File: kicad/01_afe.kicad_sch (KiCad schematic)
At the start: 0 parts

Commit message: Phase 1: sheet 1 (afe); power symbols for PGND/ISOPGND/DAB_GROUND groups on sheet 2
Co-Authored-By: Claude Fable 5.1 <noreply@anthropic.com>
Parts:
- added ACIN1, ACIN2, AFE_OUT, FILTER_IN, FILTER_OUT, J5, PE1, PE2, PE3, PE4: PIN, symbol ac_psu:PIN
- added C13, C14, C19, C20, C22, C23: 2n2, symbol ac_psu:C
- added C21, C24, C25: 7u, symbol ac_psu:C
- added C26: 100n, symbol ac_psu:C
- added CM1, CM2: WE-CMBNC, symbol ac_psu:WE-CMBNC
- added Q1, Q2, Q3, Q4: C3M0065090D, symbol ac_psu:C3M0065090D
- added R10: TWW10J15RE, symbol ac_psu:R
- added R11, R12, R13, R14, R15, R16, R2, R3, R4, R5, R6, R95: 91K, symbol ac_psu:R
- added R17, R21, R8: 10k, symbol ac_psu:R
- added R18, R9: 100, symbol ac_psu:R
- added R20: SLA-12VDC-SL-A, symbol ac_psu:SLA-12VDC-SL-A
- added R48: FKK5R0020FE-TR, symbol ac_psu:FKK5R0020FE-TR
- added R7: 1k, symbol ac_psu:R
- added U1: OPA2353UA, symbol ac_psu:OPA2353UA
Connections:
- new net: R3.1, R8.2, U1.6 (-)
- new net: R2.1, R3.2
- new net: R17.1, R18.2, U1.1
- new net: R16.1, R17.2, U1.2 (-)
- new net: R8.1, R9.2, U1.7
- new net: R12.2, R95.1
- new net: R4.1, R5.2
- new net: R15.1, R16.2
- new net: R14.1, R15.2
- new net: R12.1, R13.2
- new net: R11.1, R2.2
- new net: R6.1, R7.2, U1.5 (+)
- new net: R13.1, R21.2, U1.3 (+)
- new net: R5.1, R6.2
- new net 20V: R20.6 (COIL_2)
- new net AC_IN2: ACIN2.1, C14.2, C25.2, CM2.4, R95.2
- new net AC_IN_1: ACIN1.1, R10.1, R14.2, R20.3 (NO)
- new net ADA2: R18.1
- new net ADA3: R9.1
- new net CMFILT1: C22.2, C24.1, CM1.3, CM2.2
- new net CMFILT2: C23.2, C24.2, CM1.4, CM2.1
- new net DC+: Q1.2 (D), Q3.2 (D)
- new net FILTER_INPUT: C20.2, C21.2, CM1.1, FILTER_IN.1, R11.2
- new net G1_GATE_HI: Q1.1 (G)
- new net G1_SOURCE_HI: Q1.3 (S), Q2.2 (D), R48.4
- new net G2_GATE_LO: Q2.1 (G)
- new net G3_GATE_HI: Q3.1 (G)
- new net G3_SOURCE_HI: AFE_OUT.1, Q3.3 (S), Q4.2 (D)
- new net G4_GATE_LO: Q4.1 (G)
- new net GND: C26.1, U1.4 (V-)
- new net JEE: C13.2, C25.1, CM2.3, R10.2, R20.1 (COM_1)
- new net LEMOUT: C19.2, C21.1, CM1.2, FILTER_OUT.1, R4.2
- new net PE1: C19.1, C20.1, C23.1, PE1.1
- new net PE2: C14.1, PE2.1
- new net PE3: C22.1, PE3.1
- new net PE4: C13.1, PE4.1
- new net PGND: Q2.3 (S), Q4.3 (S)
- new net REF_1V65: R21.1, R7.1
- new net RELAY_DRIVE: R20.2 (COIL_1)
- new net SHUNT1: J5.1, R48.1, R48.3
- new net SHUNT2: R48.2
- new net VCC: C26.2, U1.8 (V+)
- no-connect marks 0 -> 1
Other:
- note added: "2 = SHUNT2 sense. U5 (sheet 8) floats on SHUNT1/SHUNT2."
- note added: "3V3 / DC- in the Proteus schematic = VCC / GND"
- note added: "AFE half bridges. Q2/Q4 sources are PGND (Proteus calls them G2_Source_LO / G4_Source_LO at J1)."
- note added: "EMI filter between the mains (ACIN1/ACIN2) and FILTER_IN/FILTER_OUT; R10 limits inrush until R20 closes."
- note added: "R48 2 mOhm shunt: 4 = Q1/Q2 midpoint, 1/3 = SHUNT1 -> J5 (afe_1_out_measured),"
- note added: "U1:A measures the mains voltage (AC_IN2 - AC_IN_1) around REF_1V65 -> ADA2."
- note added: "U1:B measures the filter voltage (LEMOUT - FILTER_INPUT) around REF_1V65 -> ADA3."

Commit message: Phase 2 done: footprints assigned and verified against IPC pads
- tools/gen_footprints.py -> lib/footprint_map.csv + lib/ac_psu.pretty (20 project footprints)
- tools/fpgeom.py: footprint pad loader and rigid fit; tools/check_footprints.py (+ pcbnew
  placement check), added to check_all.sh; reports/footprint_fit.csv for Phase 3 placement
- sch_builder: Footprint field from the map, deterministic UUIDs; all sheets regenerated
- kicad/fp-lib-table; STATUS.md (decisions, residuals, REF3025/C67 findings); Phase 3 prompt

Co-Authored-By: Claude Opus 5.5 <noreply@anthropic.com>
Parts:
- ACIN1, ACIN2: footprint (none) -> ac_psu:Terminal_2x1_P5.00mm_D2.0mm_Drill1.4mm
- AFE_OUT, FILTER_IN, FILTER_OUT, J5, PE3: footprint (none) -> ac_psu:Terminal_D4.0mm_Drill2.55mm
- C13, C14, C19, C20, C22, C23: footprint (none) -> Capacitor_THT:C_Disc_D12.5mm_W5.0mm_P7.50mm
- C21, C24, C25: footprint (none) -> Capacitor_THT:C_Rect_L33.0mm_W20.0mm_P27.50mm_MKS4
- C26: footprint (none) -> Capacitor_SMD:C_0402_1005Metric
- CM1, CM2: footprint (none) -> ac_psu:L_CommonMode_WE-CMBNC
- PE1: footprint (none) -> ac_psu:Terminal_D4.0mm_Drill3.0mm
- PE2, PE4: footprint (none) -> ac_psu:Terminal_D4.0mm_Drill2.0mm
- Q1, Q2, Q3, Q4: footprint (none) -> Package_TO_SOT_THT:TO-247-3_Vertical
- R10: footprint (none) -> Resistor_THT:R_Radial_Power_L13.0mm_W9.0mm_P5.00mm
- R11, R12, R13, R14, R15, R16, R2, R3, R4, R5, R6, R95: footprint (none) -> Resistor_SMD:R_1206_3216Metric_Pad1.30x1.75mm_HandSolder
- R17, R18, R21, R7, R8, R9: footprint (none) -> Resistor_SMD:R_0402_1005Metric
- R20: footprint (none) -> ac_psu:Relay_SLA-12VDC-SL-A
- R48: footprint (none) -> ac_psu:R_Shunt_FKK5R0020FE
- U1: footprint (none) -> Package_SO:TSSOP-8_3x3mm_P0.65mm
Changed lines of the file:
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@@
 			)
 		)
-		(property "Footprint" ""
+		(property "Footprint" "Package_TO_SOT_THT:TO-247-3_Vertical"
 			(at 55.88 48.26 0)
 			(effects
@@
 			)
 		)
-		(property "Footprint" ""
+		(property "Footprint" "Package_TO_SOT_THT:TO-247-3_Vertical"
 			(at 55.88 86.36 0)
 			(effects
@@
 			)
 		)
-		(property "Footprint" ""
+		(property "Footprint" "Package_TO_SOT_THT:TO-247-3_Vertical"
 			(at 106.68 48.26 0)
 			(effects
@@
 			)
 		)
-		(property "Footprint" ""
+		(property "Footprint" "Package_TO_SOT_THT:TO-247-3_Vertical"
 			(at 106.68 86.36 0)
 			(effects
@@
 			)
 		)
-		(property "Footprint" ""
+		(property "Footprint" "ac_psu:Terminal_D4.0mm_Drill2.55mm"
 			(at 119.38 74.93 0)
 			(effects
@@
 			)
 		)
-		(property "Footprint" ""
+		(property "Footprint" "ac_psu:R_Shunt_FKK5R0020FE"
 			(at 148.082 45.72 0)
 			(effects
@@
 			)
 		)
-		(property "Footprint" ""
+		(property "Footprint" "ac_psu:Terminal_D4.0mm_Drill2.55mm"
 			(at 160.02 48.26 0)
 			(effects
@@
 			)
 		)
-		(property "Footprint" ""
+		(property "Footprint" "ac_psu:Terminal_D4.0mm_Drill2.55mm"
 			(at 220.98 50.8 0)
 			(effects
@@
 			)
 		)
-		(property "Footprint" ""
+		(property "Footprint" "ac_psu:Terminal_D4.0mm_Drill2.55mm"
 			(at 210.82 60.96 0)
 			(effects
@@
 			)
 		)
-		(property "Footprint" ""
+		(property "Footprint" "Capacitor_THT:C_Disc_D12.5mm_W5.0mm_P7.50mm"
 			(at 224.4852 46.99 0)
 			(effects
@@
 			)
 		)
-		(property "Footprint" ""
+		(property "Footprint" "Capacitor_THT:C_Disc_D12.5mm_W5.0mm_P7.50mm"
 			(at 222.5548 64.77 0)
 			(effects
@@
 			)
 		)
-		(property "Footprint" ""
+		(property "Footprint" "Capacitor_THT:C_Rect_L33.0mm_W20.0mm_P27.50mm_MKS4"
 			(at 232.1052 59.69 0)
 			(effects
@@
 			)
 		)
-		(property "Footprint" ""
+		(property "Footprint" "ac_psu:L_CommonMode_WE-CMBNC"
 			(at 241.3 62.23 0)
 			(effects
@@
 			)
 		)
-		(property "Footprint" ""
+		(property "Footprint" "Capacitor_THT:C_Disc_D12.5mm_W5.0mm_P7.50mm"
 			(at 254.9652 46.99 0)
 			(effects
@@
 			)
 		)
-		(property "Footprint" ""
+		(property "Footprint" "Capacitor_THT:C_Disc_D12.5mm_W5.0mm_P7.50mm"
 			(at 253.0348 64.77 0)
 			(effects
@@
 			)
 		)
-		(property "Footprint" ""
+		(property "Footprint" "Capacitor_THT:C_Rect_L33.0mm_W20.0mm_P27.50mm_MKS4"
 			(at 262.5852 59.69 0)
 			(effects
@@
 			)
 		)
-		(property "Footprint" ""
+		(property "Footprint" "ac_psu:L_CommonMode_WE-CMBNC"
 			(at 271.78 62.23 0)
 			(effects
@@
 			)
 		)
-		(property "Footprint" ""
+		(property "Footprint" "Capacitor_THT:C_Rect_L33.0mm_W20.0mm_P27.50mm_MKS4"
 			(at 287.9852 59.69 0)
 			(effects
@@
 			)
 		)
-		(property "Footprint" ""
+		(property "Footprint" "Capacitor_THT:C_Disc_D12.5mm_W5.0mm_P7.50mm"
 			(at 295.6052 46.99 0)
 			(effects
@@
 			)
 		)
-		(property "Footprint" ""
+		(property "Footprint" "Capacitor_THT:C_Disc_D12.5mm_W5.0mm_P7.50mm"
 			(at 293.6748 64.77 0)
 			(effects
@@
 			)
 		)
-		(property "Footprint" ""
+		(property "Footprint" "Resistor_THT:R_Radial_Power_L13.0mm_W9.0mm_P5.00mm"
 			(at 300.482 35.56 0)
 			(effects
@@
 			)
 		)
-		(property "Footprint" ""
+		(property "Footprint" "ac_psu:Relay_SLA-12VDC-SL-A"
 			(at 274.32 22.86 0)
 			(effects
@@
 			)
 		)
-		(property "Footprint" ""
+		(property "Footprint" "ac_psu:Terminal_2x1_P5.00mm_D2.0mm_Drill1.4mm"
 			(at 312.42 25.4 0)
 			(effects
@@
 			)
 		)
-		(property "Footprint" ""
+		(property "Footprint" "ac_psu:Terminal_2x1_P5.00mm_D2.0mm_Drill1.4mm"
 			(at 312.42 66.04 0)
 			(effects
@@
 			)
 		)
-		(property "Footprint" ""
+		(property "Footprint" "Resistor_SMD:R_1206_3216Metric_Pad1.30x1.75mm_HandSolder"
 			(at 210.058 76.2 0)
 			(effects
@@
 			)
 		)
-		(property "Footprint" ""
+		(property "Footprint" "Resistor_SMD:R_1206_3216Metric_Pad1.30x1.75mm_HandSolder"
 			(at 210.058 86.36 0)
 			(effects
@@
 			)
 		)
-		(property "Footprint" ""
+		(property "Footprint" "Resistor_SMD:R_1206_3216Metric_Pad1.30x1.75mm_HandSolder"
 			(at 210.058 96.52 0)
 			(effects
@@
 			)
 		)
-		(property "Footprint" ""
+		(property "Footprint" "Resistor_SMD:R_1206_3216Metric_Pad1.30x1.75mm_HandSolder"
 			(at 202.438 76.2 0)
 			(effects
@@
 			)
 		)
-		(property "Footprint" ""
+		(property "Footprint" "Resistor_SMD:R_1206_3216Metric_Pad1.30x1.75mm_HandSolder"
 			(at 202.438 86.36 0)
 			(effects
@@
 			)
 		)
-		(property "Footprint" ""
+		(property "Footprint" "Resistor_SMD:R_1206_3216Metric_Pad1.30x1.75mm_HandSolder"
 			(at 202.438 96.52 0)
 			(effects
@@
 			)
 		)
-		(property "Footprint" ""
+		(property "Footprint" "Package_SO:TSSOP-8_3x3mm_P0.65mm"
 			(at 228.6 106.68 0)
 			(effects
@@
 			)
 		)
-		(property "Footprint" ""
+		(property "Footprint" "Resistor_SMD:R_0402_1005Metric"
 			(at 216.662 96.52 0)
 			(effects
@@
 			)
 		)
-		(property "Footprint" ""
+		(property "Footprint" "Resistor_SMD:R_0402_1005Metric"
 			(at 246.38 104.902 0)
 			(effects
@@
 			)
 		)
-		(property "Footprint" ""
+		(property "Footprint" "Resistor_SMD:R_0402_1005Metric"
 			(at 228.6 112.522 0)
 			(effects
@@
 			)
 		)
-		(property "Footprint" ""
+		(property "Footprint" "Resistor_SMD:R_1206_3216Metric_Pad1.30x1.75mm_HandSolder"
 			(at 309.118 121.92 0)
 			(effects
@@
 			)
 		)
-		(property "Footprint" ""
+		(property "Footprint" "Resistor_SMD:R_1206_3216Metric_Pad1.30x1.75mm_HandSolder"
 			(at 309.118 132.08 0)
 			(effects
@@
 			)
 		)
-		(property "Footprint" ""
+		(property "Footprint" "Resistor_SMD:R_1206_3216Metric_Pad1.30x1.75mm_HandSolder"
 			(at 309.118 142.24 0)
 			(effects
@@
 			)
 		)
-		(property "Footprint" ""
+		(property "Footprint" "Resistor_SMD:R_1206_3216Metric_Pad1.30x1.75mm_HandSolder"
 			(at 301.498 121.92 0)
 			(effects
@@
 			)
 		)
-		(property "Footprint" ""
+		(property "Footprint" "Resistor_SMD:R_1206_3216Metric_Pad1.30x1.75mm_HandSolder"
 			(at 301.498 132.08 0)
 			(effects
@@
 			)
 		)
-		(property "Footprint" ""
+		(property "Footprint" "Resistor_SMD:R_1206_3216Metric_Pad1.30x1.75mm_HandSolder"
 			(at 301.498 142.24 0)
 			(effects
@@
 			)
 		)
-		(property "Footprint" ""
+		(property "Footprint" "Package_SO:TSSOP-8_3x3mm_P0.65mm"
 			(at 327.66 152.4 0)
 			(effects
@@
 			)
 		)
-		(property "Footprint" ""
+		(property "Footprint" "Resistor_SMD:R_0402_1005Metric"
 			(at 315.722 142.24 0)
 			(effects
@@
 			)
 		)
-		(property "Footprint" ""
+		(property "Footprint" "Resistor_SMD:R_0402_1005Metric"
 			(at 345.44 150.622 0)
 			(effects
@@
 			)
 		)
-		(property "Footprint" ""
+		(property "Footprint" "Resistor_SMD:R_0402_1005Metric"
 			(at 327.66 158.242 0)
 			(effects
@@
 			)
 		)
-		(property "Footprint" ""
+		(property "Footprint" "Package_SO:TSSOP-8_3x3mm_P0.65mm"
 			(at 38.1 152.4 0)
 			(effects
@@
 			)
 		)
-		(property "Footprint" ""
+		(property "Footprint" "Capacitor_SMD:C_0402_1005Metric"
 			(at 54.9148 148.59 0)
 			(effects
@@
 			)
 		)
-		(property "Footprint" ""
+		(property "Footprint" "ac_psu:Terminal_D4.0mm_Drill3.0mm"
 			(at 20.32 190.5 0)
 			(effects
@@
 			)
 		)
-		(property "Footprint" ""
+		(property "Footprint" "ac_psu:Terminal_D4.0mm_Drill2.0mm"
 			(at 30.48 190.5 0)
 			(effects
@@
 			)
 		)
-		(property "Footprint" ""
+		(property "Footprint" "ac_psu:Terminal_D4.0mm_Drill2.55mm"
 			(at 40.64 190.5 0)
 			(effects
@@
 			)
 		)
-		(property "Footprint" ""
+		(property "Footprint" "ac_psu:Terminal_D4.0mm_Drill2.0mm"
 			(at 50.8 190.5 0)
 			(effects

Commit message: Phase 3 done: PCB rebuilt from the Proteus gerbers with nets and zones
tools/make_pcb.sh regenerates kicad/ac_psu.kicad_pcb (byte-reproducible):
build_pcb.py (footprints with nets and symbol links at the Proteus
positions, outline, mounting holes, rules), gerber_to_tracks.py (4052
tracks, 173 vias; pour edge strokes recognised and skipped),
assign_nets.py (union-find over copper, 0 shorts/orphans/opens with
pours), pours_to_zones.py (79 zones = Proteus pour copper incl. holes).

New checks in check_all.sh: check_board.py (pads/holes/vias vs IPC),
assign_nets.py --check (after zone fill), drc.py (0 shorts, 0
unconnected, 0 parity issues; courtyard overlaps accepted).

Footprints (user decision): Proteus pad sizes for the headers, TSSOP,
SOT-23(-5), SOIC-16W packages whose KiCad pads shorted/violated
clearance; Proteus pads and drills for TO-247, VXO7805, P27.5 film and
snap-in caps; tighter courtyards for IPC-built footprints.

Co-Authored-By: Claude Opus 5.5 <noreply@anthropic.com>
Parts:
- C21, C25: footprint Capacitor_THT:C_Rect_L33.0mm_W20.0mm_P27.50mm_MKS4 -> ac_psu:C_Rect_L33.0mm_W20.0mm_P27.50mm_MKS4_Proteus
- Q1, Q2, Q3, Q4: footprint Package_TO_SOT_THT:TO-247-3_Vertical -> ac_psu:TO-247-3_Vertical_Proteus
- U1: footprint Package_SO:TSSOP-8_3x3mm_P0.65mm -> ac_psu:TSSOP-8_3x3mm_P0.65mm_Proteus
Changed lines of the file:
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@@
 			)
 		)
-		(property "Footprint" "Package_TO_SOT_THT:TO-247-3_Vertical"
+		(property "Footprint" "ac_psu:TO-247-3_Vertical_Proteus"
 			(at 55.88 48.26 0)
 			(effects
@@
 			)
 		)
-		(property "Footprint" "Package_TO_SOT_THT:TO-247-3_Vertical"
+		(property "Footprint" "ac_psu:TO-247-3_Vertical_Proteus"
 			(at 55.88 86.36 0)
 			(effects
@@
 			)
 		)
-		(property "Footprint" "Package_TO_SOT_THT:TO-247-3_Vertical"
+		(property "Footprint" "ac_psu:TO-247-3_Vertical_Proteus"
 			(at 106.68 48.26 0)
 			(effects
@@
 			)
 		)
-		(property "Footprint" "Package_TO_SOT_THT:TO-247-3_Vertical"
+		(property "Footprint" "ac_psu:TO-247-3_Vertical_Proteus"
 			(at 106.68 86.36 0)
 			(effects
@@
 			)
 		)
-		(property "Footprint" "Capacitor_THT:C_Rect_L33.0mm_W20.0mm_P27.50mm_MKS4"
+		(property "Footprint" "ac_psu:C_Rect_L33.0mm_W20.0mm_P27.50mm_MKS4_Proteus"
 			(at 232.1052 59.69 0)
 			(effects
@@
 			)
 		)
-		(property "Footprint" "Capacitor_THT:C_Rect_L33.0mm_W20.0mm_P27.50mm_MKS4"
+		(property "Footprint" "ac_psu:C_Rect_L33.0mm_W20.0mm_P27.50mm_MKS4_Proteus"
 			(at 287.9852 59.69 0)
 			(effects
@@
 			)
 		)
-		(property "Footprint" "Package_SO:TSSOP-8_3x3mm_P0.65mm"
+		(property "Footprint" "ac_psu:TSSOP-8_3x3mm_P0.65mm_Proteus"
 			(at 228.6 106.68 0)
 			(effects
@@
 			)
 		)
-		(property "Footprint" "Package_SO:TSSOP-8_3x3mm_P0.65mm"
+		(property "Footprint" "ac_psu:TSSOP-8_3x3mm_P0.65mm_Proteus"
 			(at 327.66 152.4 0)
 			(effects
@@
 			)
 		)
-		(property "Footprint" "Package_SO:TSSOP-8_3x3mm_P0.65mm"
+		(property "Footprint" "ac_psu:TSSOP-8_3x3mm_P0.65mm_Proteus"
 			(at 38.1 152.4 0)
 			(effects

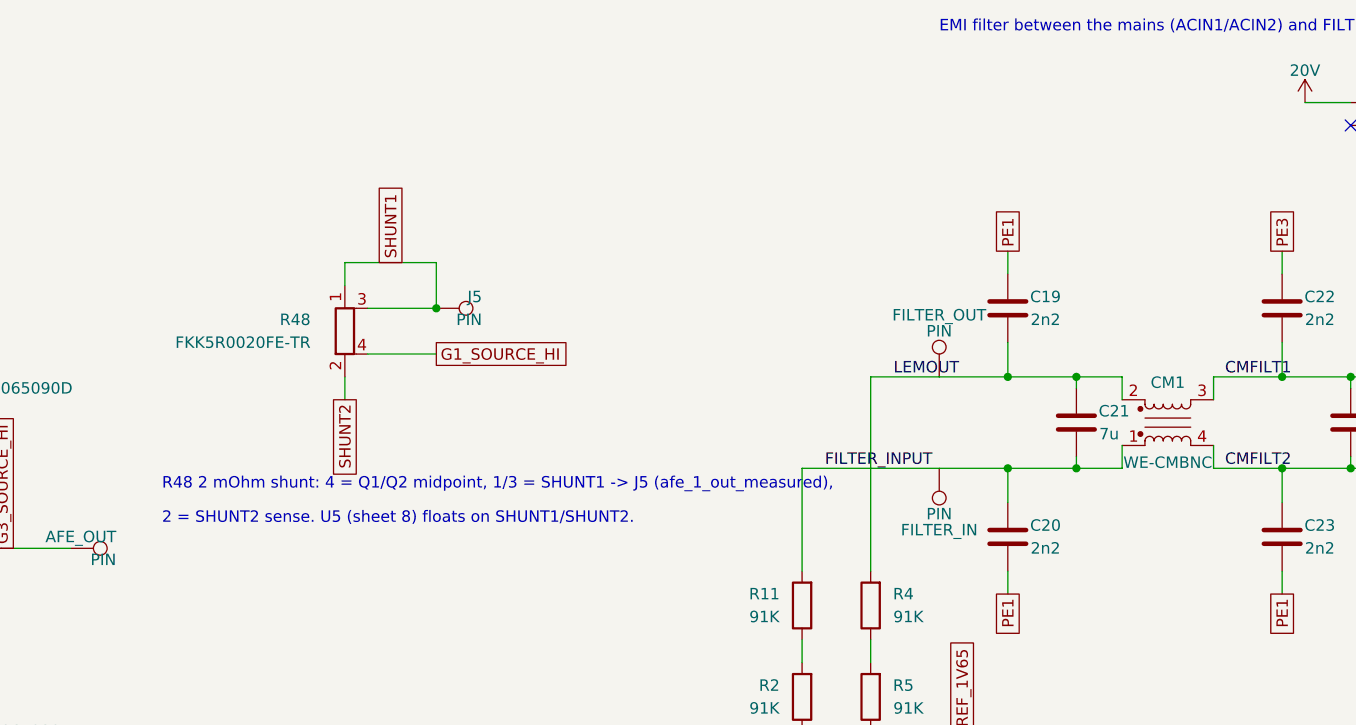
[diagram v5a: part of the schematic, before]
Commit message: v4 design fixes: RET_ISO->ISOGND, U11 INH->GND, C88/C89 on ADA2/ADA3, ADuM7701 RC compensation, R48 Kelvin split
Board frozen: kicad/ac_psu.kicad_pcb edited by one-shot pcbnew scripts tools/v4/fix_1..5
(apply_all.sh, reproducible from the tag's board); make_pcb.sh rebuilds the Proteus board from
tag proteus-conversion-complete into build/proteus/ (byte-identical, checked by regen_check).
Proteus comparisons apply exactly lib/v4_deviations.csv + lib/v4_copper.csv (tools/deviations.py,
wrappers compare_netlists_v4 / check_symbols_v4, deviation support in check_board,
check_footprints, gen_footprints, ipc356_diff, gerber_roundtrip). p2k submodule unchanged.
check_all: ALL CHECKS PASSED; DRC 0 shorts / 0 unconnected / 0 parity (+1 accepted courtyard
overlap C91/U5).

Co-Authored-By: Claude Opus 5.5 <noreply@anthropic.com>
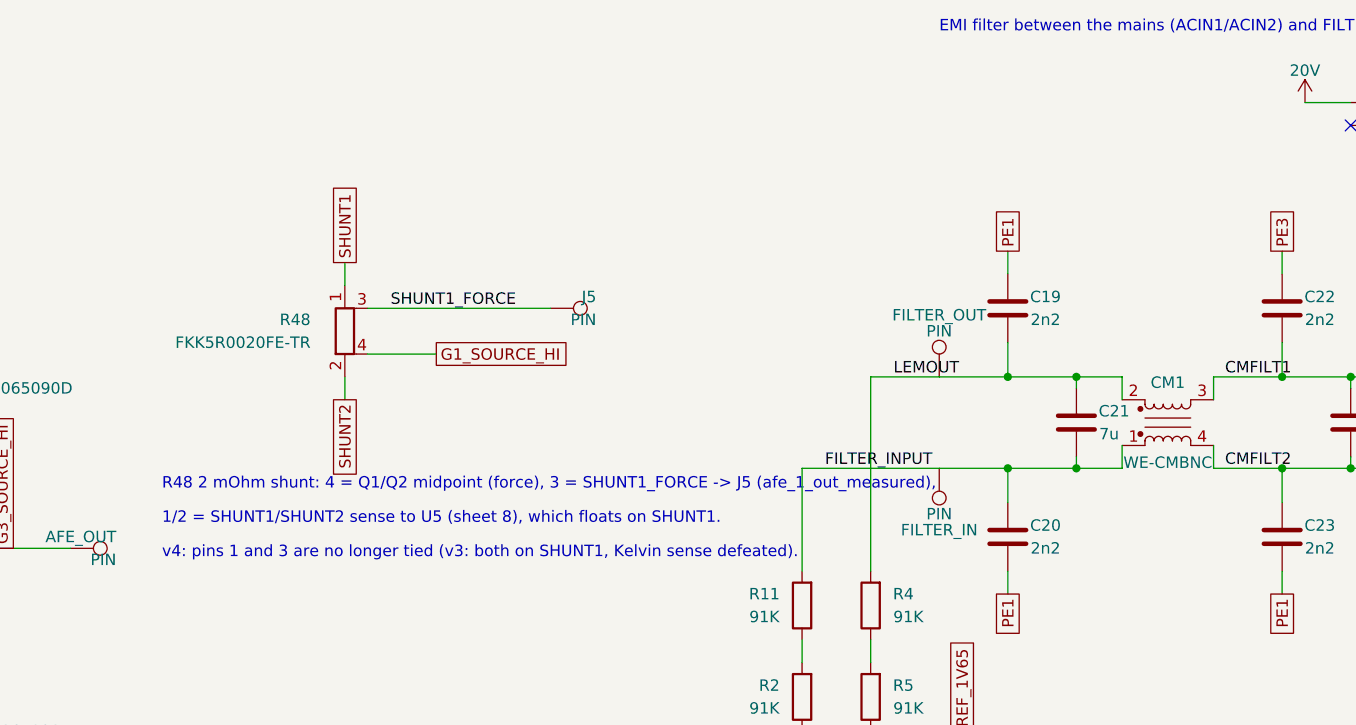
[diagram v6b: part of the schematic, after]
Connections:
- net SHUNT1: no longer J5.1, R48.3
- new net SHUNT1_FORCE: J5.1, R48.3
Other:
- note added: "1/2 = SHUNT1/SHUNT2 sense to U5 (sheet 8), which floats on SHUNT1."
- note added: "R48 2 mOhm shunt: 4 = Q1/Q2 midpoint (force), 3 = SHUNT1_FORCE -> J5 (afe_1_out_measured),"
- note added: "v4: pins 1 and 3 are no longer tied (v3: both on SHUNT1, Kelvin sense defeated)."
- note removed: "2 = SHUNT2 sense. U5 (sheet 8) floats on SHUNT1/SHUNT2."
- note removed: "R48 2 mOhm shunt: 4 = Q1/Q2 midpoint, 1/3 = SHUNT1 -> J5 (afe_1_out_measured),"
- moved on the sheet: J5
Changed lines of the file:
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@@
-		)
-	)
-	(wire
-		(pts
-			(xy 149.86 38.1) (xy 160.02 38.1)
-		)
-		(stroke
-			(width 0)
-			(type default)
-		)
-	)
-	(wire
-		(pts
-			(xy 160.02 38.1) (xy 160.02 43.18)
-		)
-		(stroke
-			(width 0)
-			(type default)
 		)
 	)
 	(global_label "SHUNT1"
 		(shape passive)
-		(at 154.94 38.1 90)
+		(at 149.86 38.1 90)
 		(fields_autoplaced yes)
 		(effects
@@
 		)
 		(property "Intersheetrefs" "${INTERSHEET_REFS}"
-			(at 154.94 38.1 0)
+			(at 149.86 38.1 0)
 			(effects
 				(font
@@
 	(wire
 		(pts
-			(xy 152.4 43.18) (xy 160.02 43.18)
+			(xy 152.4 43.18) (xy 172.72 43.18)
 		)
 		(stroke
@@
 		)
 	)
-	(junction
-		(at 160.02 43.18)
-		(diameter 0)
-		(color 0 0 0 0)
-	)
 	(symbol
 		(lib_id "ac_psu:PIN")
-		(at 160.02 43.18 270)
+		(at 172.72 43.18 270)
 		(unit 1)
 		(exclude_from_sim no)
@@
 		(dnp no)
 		(property "Reference" "J5"
-			(at 165.1 41.91 90)
+			(at 177.8 41.91 90)
 			(effects
 				(font
@@
 		)
 		(property "Value" "PIN"
-			(at 165.1 44.45 90)
+			(at 177.8 44.45 90)
 			(effects
 				(font
@@
 		)
 		(property "Footprint" "ac_psu:Terminal_D4.0mm_Drill2.55mm"
-			(at 160.02 48.26 0)
+			(at 172.72 48.26 0)
 			(effects
 				(font
@@
 		)
 		(property "Datasheet" ""
-			(at 160.02 48.26 0)
+			(at 172.72 48.26 0)
 			(effects
 				(font
@@
 		)
 		(property "Description" "Proteus PIN terminal (single pad; ACIN/ACOUT footprints have two pads numbered 1)"
-			(at 160.02 43.18 0)
+			(at 172.72 43.18 0)
 			(effects
 				(font
@@
 				)
 			)
+		)
+	)
+	(label "SHUNT1_FORCE"
+		(at 154.94 43.18 0)
+		(effects
+			(font
+				(size 1.27 1.27)
+			)
+			(justify left bottom)
 		)
 	)
@@
 		)
 	)
-	(text "R48 2 mOhm shunt: 4 = Q1/Q2 midpoint, 1/3 = SHUNT1 -> J5 (afe_1_out_measured),"
+	(text "R48 2 mOhm shunt: 4 = Q1/Q2 midpoint (force), 3 = SHUNT1_FORCE -> J5 (afe_1_out_measured),"
 		(exclude_from_sim no)
 		(at 129.54 63.5 0)
@@
 		)
 	)
-	(text "2 = SHUNT2 sense. U5 (sheet 8) floats on SHUNT1/SHUNT2."
+	(text "1/2 = SHUNT1/SHUNT2 sense to U5 (sheet 8), which floats on SHUNT1."
 		(exclude_from_sim no)
 		(at 129.54 67.31 0)
 		(effects
 			(font
+				(size 1.27 1.27)
+			)
+			(justify left bottom)
+		)
+	)
+	(text "v4: pins 1 and 3 are no longer tied (v3: both on SHUNT1, Kelvin sense defeated)."
+		(exclude_from_sim no)
+		(at 129.54 71.12 0)
+		(effects
+			(font
